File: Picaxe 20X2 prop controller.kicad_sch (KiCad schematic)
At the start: 57 parts, among them J1 FC68131, J10 Conn_01x05_Male (- power bus), J11 Conn_01x08_Male - pin I/O, J12 MP3 player, J13 servo 2, J14 servo 3, J15 servo 4, J16 servo 5, J17 Ext servo power, J18 Servo power select, J19 C.0, J2 Conn_01x08_Male - pin I/O, J20 C.5, J21 C.1, J22 C.6, J23 C.2, J24 C.7, J25 C.3, J26 C.4, J27 B.6 TX, J28 Screw_Terminal_01x06, J29 OSTTC020162, J3 servo 1, J4 servo 6, J5 B.7 RX, J6 OSTTC080162, J7 OSTTC020162, J8 PJ-202AH, J9 Conn_01x05_Male (+ power bus), U1 Picaxe 20X2, U3 L7805CV, U4 ULN2803A

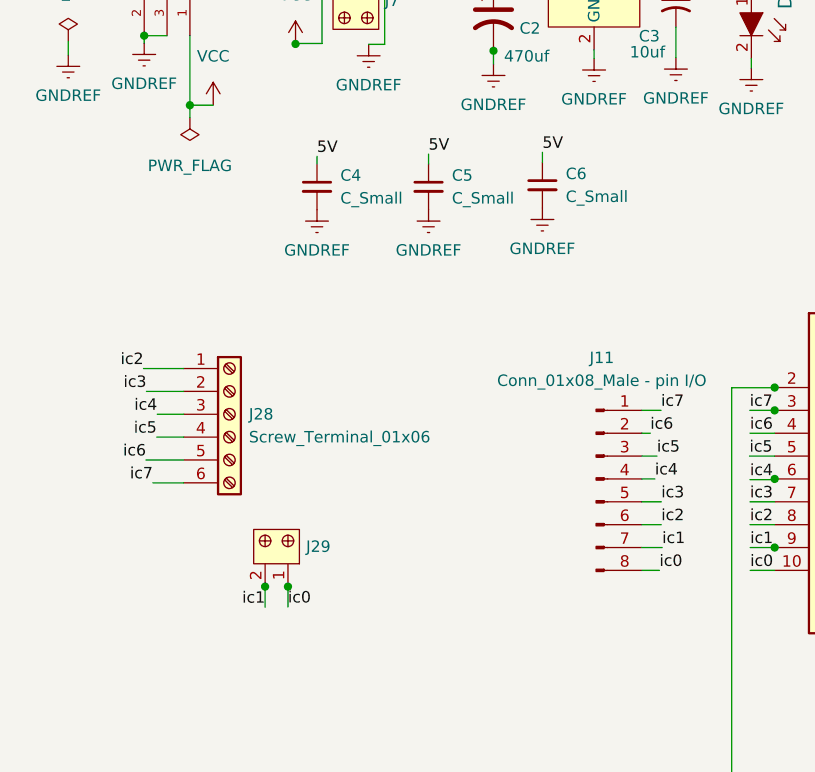
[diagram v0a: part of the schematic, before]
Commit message: added the 8 pin terminal block to the inputs
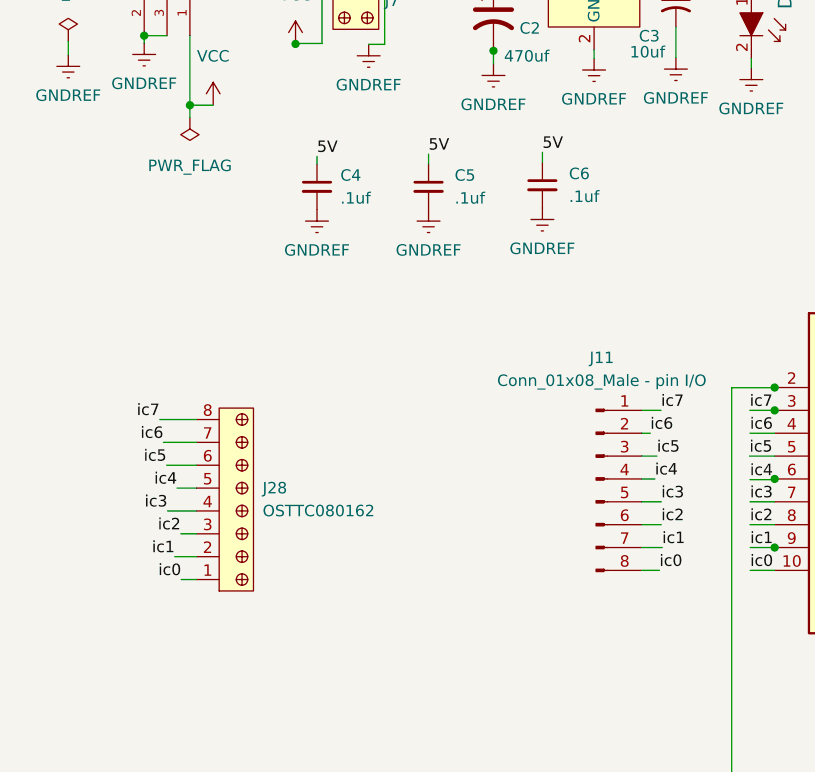
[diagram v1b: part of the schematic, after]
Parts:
- removed J28: Screw_Terminal_01x06, digikey-footprints:Term_Block_1x6_P5.08mm, symbol Connector:Screw_Terminal_01x06
- removed J29: OSTTC020162, digikey-footprints:Term_Block_1x2_P5mm, symbol dk_Terminal-Blocks-Wire-to-Board:OSTTC020162
- added J28: OSTTC080162, digikey-footprints:Term_Block_1x8_P5mm, symbol dk_Terminal-Blocks-Wire-to-Board:OSTTC080162
- C4, C5, C6: value C_Small -> .1uf
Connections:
- net ic0: now also J28.1
- net ic1: now also J28.2
- net ic2: now also J28.3
- net ic3: now also J28.4
- net ic4: now also J28.5
- net ic5: now also J28.6
- net ic6: now also J28.7
- net ic7: now also J28.8

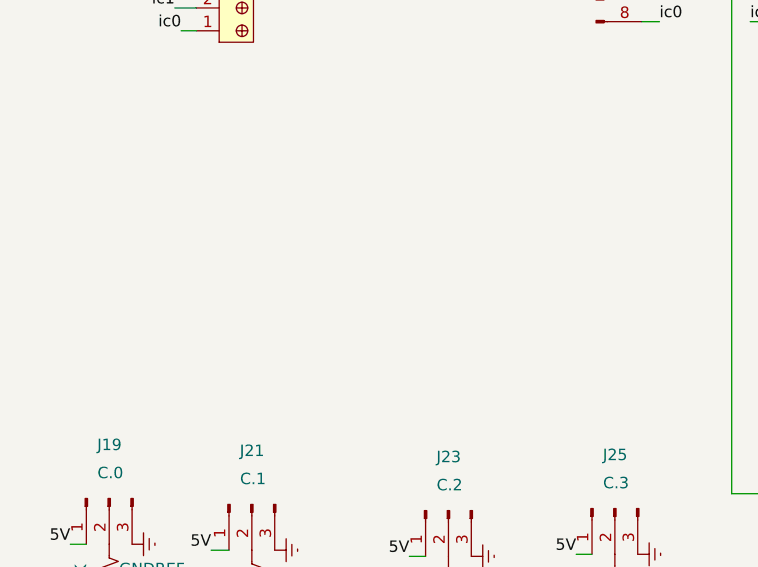
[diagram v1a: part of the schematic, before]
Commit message: forgot to save the schematic file after added the peizo and jumper
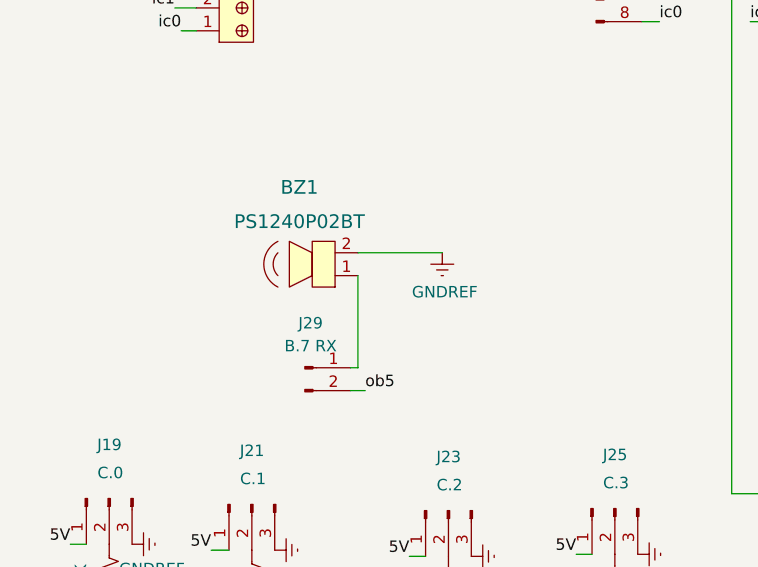
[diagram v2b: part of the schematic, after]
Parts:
- added BZ1: PS1240P02BT, digikey-footprints:Piezo_Transducer_THT_PS1240P02BT, symbol dk_Alarms-Buzzers-and-Sirens:PS1240P02BT
- added J29: B.7 RX, Connector_PinHeader_2.54mm:PinHeader_1x02_P2.54mm_Vertical, symbol Connector:Conn_01x02_Male
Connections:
- net GNDREF: now also BZ1.2
- net ob5: now also J29.2 (Pin_2)
- new net: BZ1.1, J29.1 (Pin_1)
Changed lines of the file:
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@@
+    (stroke (width 0) (type default) (color 0 0 0 0))
+  )
+  (wire (pts (xy 48.133 129.2606) (xy 49.7586 129.2606))
     (stroke (width 0) (type default) (color 0 0 0 0))
   )
@@
     (stroke (width 0) (type default) (color 0 0 0 0))
   )
+  (wire (pts (xy 48.9458 126.7206) (xy 48.9458 116.4844))
+    (stroke (width 0) (type default) (color 0 0 0 0))
+  )
   (wire (pts (xy 77.4954 155.067) (xy 80.4164 155.067))
     (stroke (width 0) (type default) (color 0 0 0 0))
@@
     (stroke (width 0) (type default) (color 0 0 0 0))
   )
+  (wire (pts (xy 48.9458 113.9444) (xy 58.3184 113.9444))
+    (stroke (width 0) (type default) (color 0 0 0 0))
+  )
   (wire (pts (xy 95.25 67.9704) (xy 90.4748 67.9704))
     (stroke (width 0) (type default) (color 0 0 0 0))
@@
   )
   (wire (pts (xy 160.4264 107.4928) (xy 160.4264 51.2572))
+    (stroke (width 0) (type default) (color 0 0 0 0))
+  )
+  (wire (pts (xy 48.133 126.7206) (xy 48.9458 126.7206))
     (stroke (width 0) (type default) (color 0 0 0 0))
   )
@@
   )
   (label "5V" (at 172.5676 163.8046 0)
+    (effects (font (size 1.27 1.27)) (justify left bottom))
+  )
+  (label "ob5" (at 49.7586 129.2606 0)
     (effects (font (size 1.27 1.27)) (justify left bottom))
   )
@@
     (pin "3")
   )
+  (symbol (lib_id "Connector:Conn_01x02_Male") (at 43.053 126.7206 0) (unit 1)
+    (in_bom yes) (on_board yes) (fields_autoplaced)
+    (property "Reference" "J29" (id 0) (at 43.688 121.7676 0))
+    (property "Value" "B.7 RX" (id 1) (at 43.688 124.3076 0))
+    (property "Footprint" "Connector_PinHeader_2.54mm:PinHeader_1x02_P2.54mm_Vertical" (id 2) (at 43.053 126.7206 0)
+      (effects (font (size 1.27 1.27)) hide)
+    )
+    (property "Datasheet" "~" (id 3) (at 43.053 126.7206 0)
+      (effects (font (size 1.27 1.27)) hide)
+    )
+    (pin "1")
+    (pin "2")
+  )
   (symbol (lib_id "Device:R_US") (at 114.5032 140.716 270) (unit 1)
     (in_bom yes) (on_board yes) (fields_autoplaced)
@@
     (pin "1")
   )
+  (symbol (lib_id "dk_Alarms-Buzzers-and-Sirens:PS1240P02BT") (at 46.4058 113.9444 180) (unit 1)
+    (in_bom yes) (on_board yes) (fields_autoplaced)
+    (property "Reference" "BZ1" (id 0) (at 42.4459 106.68 0)
+      (effects (font (size 1.524 1.524)))
+    )
+    (property "Value" "PS1240P02BT" (id 1) (at 42.4459 110.49 0)
+      (effects (font (size 1.524 1.524)))
+    )
+    (property "Footprint" "digikey-footprints:Piezo_Transducer_THT_PS1240P02BT" (id 2) (at 41.3258 119.0244 0)
+      (effects (font (size 1.524 1.524)) (justify left) hide)
+    )
+    (property "Datasheet" "https://product.tdk.com/info/en/catalog/datasheets/piezoelectronic_buzzer_ps_en.pdf" (id 3) (at 41.3258 121.5644 0)
+      (effects (font (size 1.524 1.524)) (justify left) hide)
+    )
+    (property "Digi-Key_PN" "445-2525-1-ND" (id 4) (at 41.3258 124.1044 0)
+      (effects (font (size 1.524 1.524)) (justify left) hide)
+    )
+    (property "MPN" "PS1240P02BT" (id 5) (at 41.3258 126.6444 0)
+      (effects (font (size 1.524 1.524)) (justify left) hide)
+    )
+    (property "Category" "Audio Products" (id 6) (at 41.3258 129.1844 0)
+      (effects (font (size 1.524 1.524)) (justify left) hide)
+    )
+    (property "Family" "Alarms, Buzzers, and Sirens" (id 7) (at 41.3258 131.7244 0)
+      (effects (font (size 1.524 1.524)) (justify left) hide)
+    )
+    (property "DK_Datasheet_Link" "https://product.tdk.com/info/en/catalog/datasheets/piezoelectronic_buzzer_ps_en.pdf" (id 8) (at 41.3258 134.2644 0)
+      (effects (font (size 1.524 1.524)) (justify left) hide)
+    )
+    (property "DK_Detail_Page" "/product-detail/en/tdk-corporation/PS1240P02BT/445-2525-1-ND/935930" (id 9) (at 41.3258 136.8044 0)
+      (effects (font (size 1.524 1.524)) (justify left) hide)
+    )
+    (property "Description" "AUDIO PIEZO TRANSDUCER 30V TH" (id 10) (at 41.3258 139.3444 0)
+      (effects (font (size 1.524 1.524)) (justify left) hide)
+    )
+    (property "Manufacturer" "TDK Corporation" (id 11) (at 41.3258 141.8844 0)
+      (effects (font (size 1.524 1.524)) (justify left) hide)
+    )
+    (property "Status" "Active" (id 12) (at 41.3258 144.4244 0)
+      (effects (font (size 1.524 1.524)) (justify left) hide)
+    )
+    (pin "1")
+    (pin "2")
+  )
   (symbol (lib_id "dk_Terminal-Blocks-Wire-to-Board:OSTTC020162") (at 47.4472 26.8732 0) (unit 1)
     (in_bom yes) (on_board yes) (fields_autoplaced)
@@
     (pin "1")
     (pin "2")
+  )
+  (symbol (lib_id "power:GNDREF") (at 58.3184 113.9444 0) (unit 1)
+    (in_bom yes) (on_board yes)
+    (property "Reference" "#PWR08" (id 0) (at 58.3184 120.2944 0)
+      (effects (font (size 1.27 1.27)) hide)
+    )
+    (property "Value" "GNDREF" (id 1) (at 58.5978 118.3132 0))
+    (property "Footprint" "" (id 2) (at 58.3184 113.9444 0)
+      (effects (font (size 1.27 1.27)) hide)
+    )
+    (property "Datasheet" "" (id 3) (at 58.3184 113.9444 0)
+      (effects (font (size 1.27 1.27)) hide)
+    )
+    (pin "1")
   )
   (symbol (lib_id "power:GNDREF") (at 180.6702 160.147 0) (unit 1)
@@
       (reference "#PWR07") (unit 1) (value "GNDREF") (footprint "")
     )
+    (path "/d805fea6-1393-40cf-84f8-21fd50f46bf3"
+      (reference "#PWR08") (unit 1) (value "GNDREF") (footprint "")
+    )
     (path "/afcb086b-a91e-4c22-a67a-e2359a52cea8"
       (reference "#PWR0101") (unit 1) (value "GNDREF") (footprint "")
@@
       (reference "#PWR0124") (unit 1) (value "GNDREF") (footprint "")
     )
+    (path "/cd32adbb-b86c-4eee-aa17-84272d12d149"
+      (reference "BZ1") (unit 1) (value "PS1240P02BT") (footprint "digikey-footprints:Piezo_Transducer_THT_PS1240P02BT")
+    )
     (path "/28296e28-5a7a-4d1a-b182-7a05ff4972ff"
       (reference "C1") (unit 1) (value "0.1uF") (footprint "Capacitor_THT:C_Disc_D5.0mm_W2.5mm_P5.00mm")
@@
       (reference "J28") (unit 1) (value "OSTTC080162") (footprint "digikey-footprints:Term_Block_1x8_P5mm")
     )
+    (path "/8cff5ea7-0334-4bd2-bacf-ce1263485c66"
+      (reference "J29") (unit 1) (value "B.7 RX") (footprint "Connector_PinHeader_2.54mm:PinHeader_1x02_P2.54mm_Vertical")
+    )
     (path "/9888f711-8e3e-4dbd-bfe7-1ea53137ef53"
